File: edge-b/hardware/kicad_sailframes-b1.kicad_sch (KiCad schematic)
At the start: 77 parts, among them J10 I2C_EXP1, J11 I2C_EXP2, J12 I2C_EXP3, J13 GPIO_EXP, J14 UART_DBG, J2 JST_PH_BAT, J3 U.FL, J5 MICROSD, J8 BNO085_SOCKET, J9 HOSYOND_3.5_TFT, U1 LC29HEAMD, U2 TP4056, U3 MT3608, U4 ESP32_DEVKIT_V1

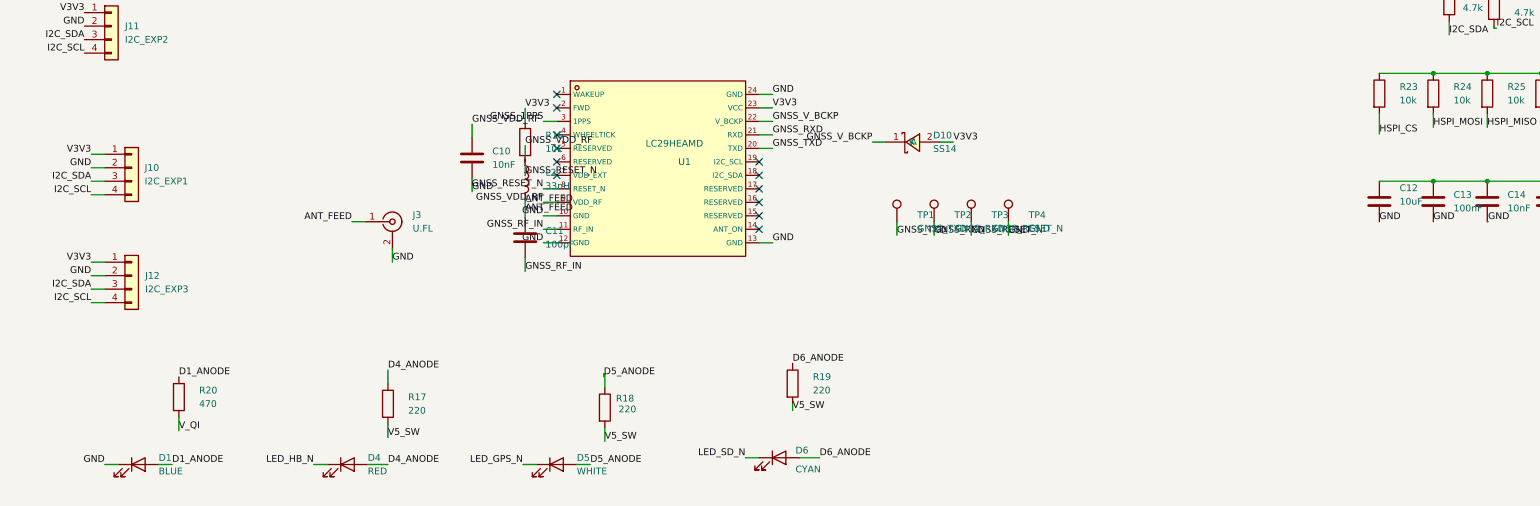
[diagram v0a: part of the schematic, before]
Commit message: B1 schematic + spec: add J15 J_AUX consolidated 1x6 expansion header
J15 (J_AUX) consolidates V3V3 + GND + I2C + UART on a single 6-pin male
2.54mm vertical pin header. Use case: connect an external expansion
module that needs both I2C and UART with a single 6-conductor cable.

Pin map:
  1. V3V3
  2. GND
  3. I2C_SDA (shared bus with BNO085 and J10-J12)
  4. I2C_SCL (shared bus)
  5. RX0 (UART0 RX, GPIO3 - shared with J14 and USB-C, mutually exclusive)
  6. TX0 (UART0 TX, GPIO1 - shared with J14 and USB-C)

Added Conn_01x06 lib_symbol def to lib_symbols. J15 instance placed at
canvas (210, 240) with wire-stub-to-label pattern (6 wires, 6 labels).

Also restored U4 ESP32 footprint reference back to b1_Library:ESP32DEVIKITV1
(reverted from ESP32-footprints-Lib:ESP32DEVKITV1 that got re-introduced
by an Update-Symbol-from-Library action). NOTE: do not run "Update Symbol
from Library" on U4 — it pulls a non-existent footprint reference back.

ERC: 0 errors, 0 warnings.

Co-Authored-By: Claude Opus 4.7 (1M context) <noreply@anthropic.com>
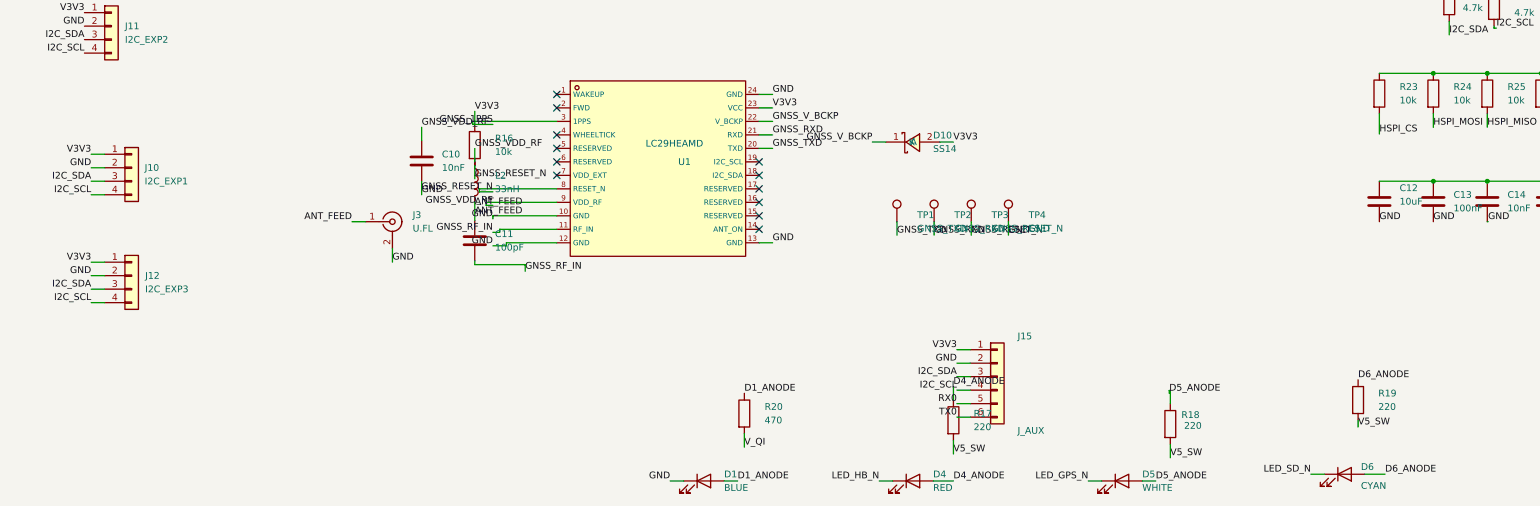
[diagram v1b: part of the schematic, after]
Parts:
- added J15: J_AUX, Connector_PinHeader_2.54mm:PinHeader_1x06_P2.54mm_Vertical, symbol Connector_Generic:Conn_01x06
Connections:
- net GND: now also J15.2 (Pin_2)
- net I2C_SCL: now also J15.4 (Pin_4)
- net I2C_SDA: now also J15.3 (Pin_3)
- net RX0: now also J15.5 (Pin_5)
- net TX0: now also J15.6 (Pin_6)
- net V3V3: now also J15.1 (Pin_1)
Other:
- moved on the sheet: C10, C11, D1, D4, D5, D6, L2, R16, R17, R18, R19, R20

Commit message: B1: J15 J_AUX final pin map — V3V3/GND/I2C/AUX_INT/V5_SW
User-corrected J15 pin layout to support mixed-voltage I²C expansion
modules with interrupt line:

Pin map (replacing the earlier RX0/TX0 assignment):
  1. V3V3           (3.3 V power)
  2. GND
  3. I2C_SDA        (shared bus)
  4. I2C_SCL        (shared bus)
  5. AUX_INT        (GPIO36 / SVP / ADC1_CH0, input-only)
  6. V5_SW          (5 V switched rail from MT3608 boost)

Use cases: KY-038 sound sensor (5 V + digital INT), RM3100 magnetometer
(I²C + DRDY), DPS310/BMP388 (I²C), any future I²C device with an INT line.

Renamed net GPIO36 → AUX_INT on J13 pin 3 and U4 pin 2 to match the new
descriptive name. J14 RX0/TX0 unchanged — UART0 debug header still
separately available.

Spec doc updated with KY-038 / RM3100 use cases and the V3V3/V5_SW
mixed-voltage warning.

ERC: 0 errors, 0 warnings.

Co-Authored-By: Claude Opus 4.7 (1M context) <noreply@anthropic.com>
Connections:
- net RX0: no longer J15.5 (Pin_5)
- net TX0: no longer J15.6 (Pin_6)
- net V5_SW: now also J15.6 (Pin_6)
- net GPIO36 renamed AUX_INT
- net AUX_INT: now also J15.5 (Pin_5)
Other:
- moved on the sheet: J15
